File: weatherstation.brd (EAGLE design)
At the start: 83 x 82 mm, 62 parts, among them CON1 USBC, CON2 DC-005, CON3 LCD-TFT, CON4 ST-LINK, CON5 TEST, CON6 BME680, T1 2N7002, T2 2N7002, T3 2N7002, T4 2N7002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

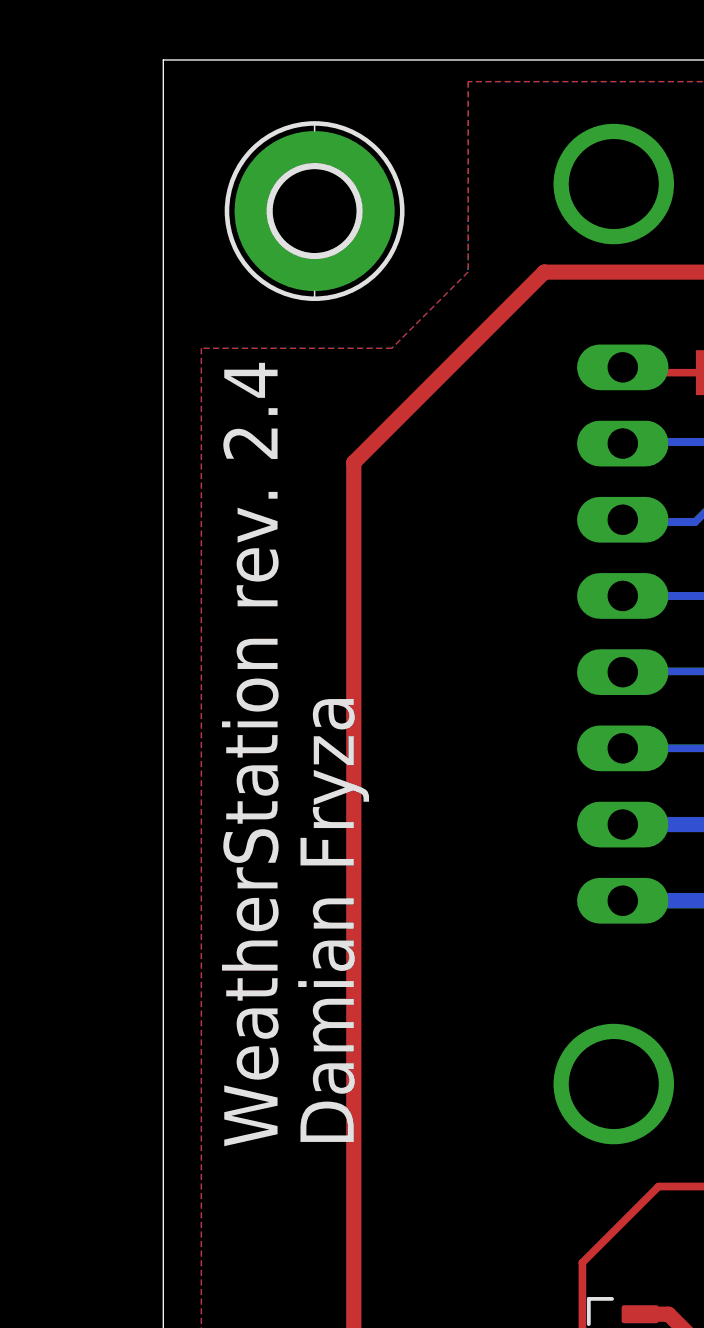
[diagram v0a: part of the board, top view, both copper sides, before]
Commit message: Changing wrong rev
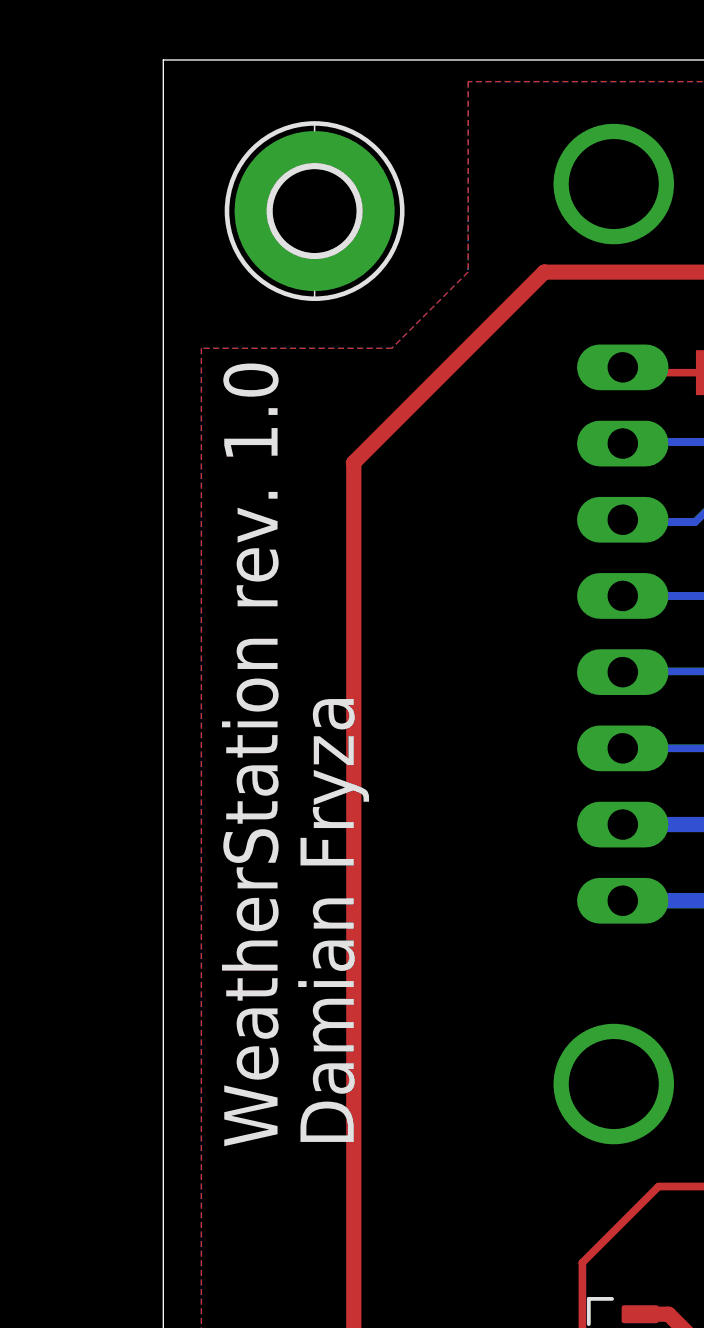
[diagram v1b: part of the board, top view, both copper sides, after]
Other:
- board text added: "WeatherStation rev. 1.0"
- board text removed: "WeatherStation rev. 2.4"
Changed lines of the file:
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@@
 <wire x1="0" y1="82" x2="0" y2="0" width="0" layer="20"/>
 <text x="6.35" y="45.72" size="1.778" layer="21" rot="R90">Damian Fryza</text>
-<text x="3.81" y="45.72" size="1.778" layer="21" rot="R90">WeatherStation rev. 2.4</text>
+<text x="3.81" y="45.72" size="1.778" layer="21" rot="R90">WeatherStation rev. 1.0</text>
 <text x="76.2" y="24.13" size="1.524" layer="25" rot="R90">VDD</text>
 <text x="76.2" y="18.3642" size="1.524" layer="25" rot="R90">PA6</text>
